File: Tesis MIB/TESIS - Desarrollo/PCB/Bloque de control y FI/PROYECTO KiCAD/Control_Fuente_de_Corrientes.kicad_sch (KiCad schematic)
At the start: 1 part, among them J1 AudioJack2

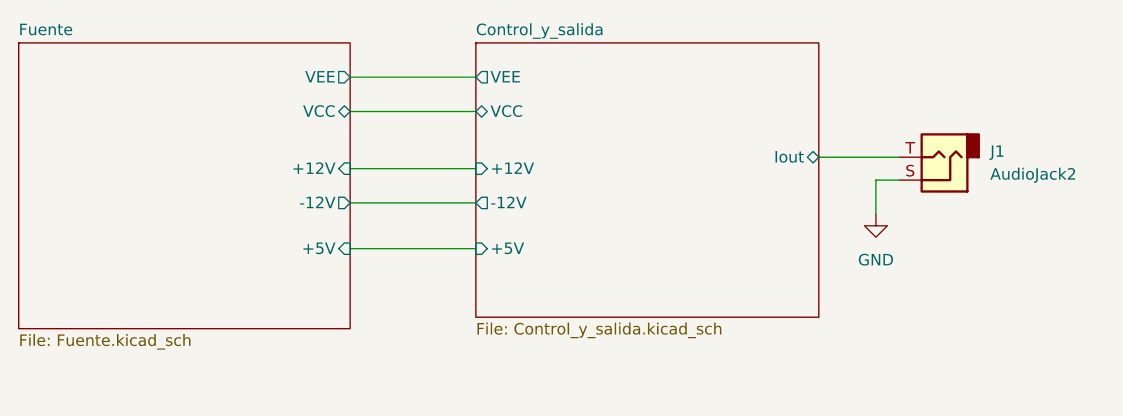
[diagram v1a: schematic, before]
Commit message: Actualiza Pruebas
Agrega planilla, gráficos y capturas del osciloscopio para el CAP3
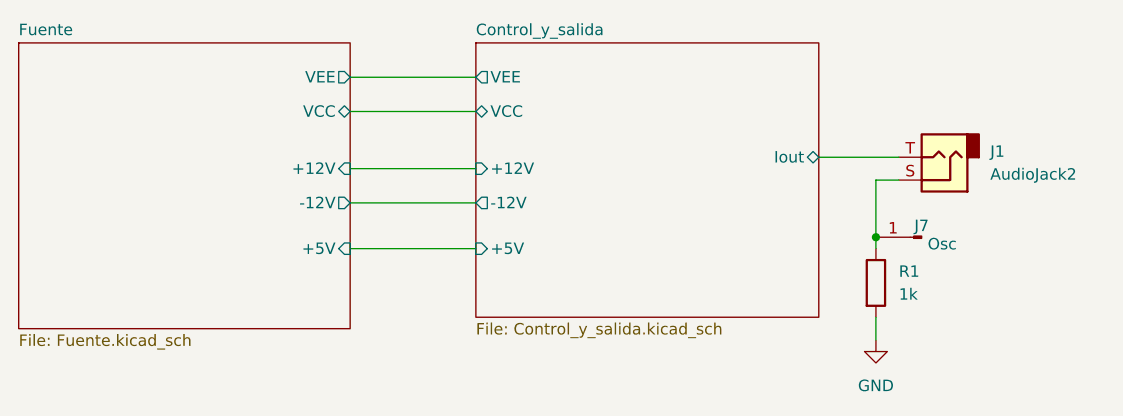
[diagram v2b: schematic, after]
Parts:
- added J7: Osc, Connector_Pin:Pin_D0.9mm_L10.0mm_W2.4mm_FlatFork, symbol Connector:Conn_01x01_Male
- added R1: 1k, Resistor_THT:R_Axial_DIN0207_L6.3mm_D2.5mm_P10.16mm_Horizontal, symbol Device:R
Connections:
- net GND: now also R1.2; no longer J1.S
- new net: J1.S, J7.1 (Pin_1), R1.1
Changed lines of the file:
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@@
 		(comment 2 "Tesis MIB: García Cabrera, Jeremías A.")
 	)
-	(wire
-		(pts
-			(xy 214.63 83.82) (xy 214.63 87.63)
+	(junction
+		(at 214.63 90.17)
+		(diameter 0)
+		(color 0 0 0 0)
+	)
+	(wire
+		(pts
+			(xy 214.63 90.17) (xy 214.63 91.44)
+		)
+		(stroke
+			(width 0)
+			(type default)
+		)
+	)
+	(wire
+		(pts
+			(xy 214.63 99.06) (xy 214.63 101.6)
 		)
 		(stroke
@@
 			(width 0)
 			(type default)
+		)
+	)
+	(wire
+		(pts
+			(xy 214.63 83.82) (xy 214.63 90.17)
+		)
+		(stroke
+			(width 0)
+			(type default)
+		)
+	)
+	(symbol
+		(lib_id "Device:R")
+		(at 214.63 95.25 0)
+		(unit 1)
+		(exclude_from_sim no)
+		(in_bom yes)
+		(on_board yes)
+		(dnp no)
+		(fields_autoplaced yes)
+		(property "Reference" "R1"
+			(at 217.17 93.9799 0)
+			(effects
+				(font
+					(size 1.27 1.27)
+				)
+				(justify left)
+			)
+		)
+		(property "Value" "1k"
+			(at 217.17 96.5199 0)
+			(effects
+				(font
+					(size 1.27 1.27)
+				)
+				(justify left)
+			)
+		)
+		(property "Footprint" "Resistor_THT:R_Axial_DIN0207_L6.3mm_D2.5mm_P10.16mm_Horizontal"
+			(at 212.852 95.25 90)
+			(effects
+				(font
+					(size 1.27 1.27)
+				)
+				(hide yes)
+			)
+		)
+		(property "Datasheet" "~"
+			(at 214.63 95.25 0)
+			(effects
+				(font
+					(size 1.27 1.27)
+				)
+				(hide yes)
+			)
+		)
+		(property "Description" "Shunt"
+			(at 214.63 95.25 0)
+			(effects
+				(font
+					(size 1.27 1.27)
+				)
+				(hide yes)
+			)
+		)
+		(pin "1"
+		)
+		(pin "2"
+		)
+		(instances
+			(project "Control_Fuente_de_Corrientes"
+				(path "/d8b362ed-b66b-443a-9ff8-8e45e9f3933f"
+					(reference "R1")
+					(unit 1)
+				)
+			)
+		)
+	)
+	(symbol
+		(lib_id "Connector:Conn_01x01_Male")
+		(at 219.71 90.17 180)
+		(unit 1)
+		(exclude_from_sim no)
+		(in_bom yes)
+		(on_board yes)
+		(dnp no)
+		(property "Reference" "J7"
+			(at 219.71 88.9 0)
+			(effects
+				(font
+					(size 1.27 1.27)
+				)
+			)
+		)
+		(property "Value" "Osc"
+			(at 221.996 90.932 0)
+			(effects
+				(font
+					(size 1.27 1.27)
+				)
+			)
+		)
+		(property "Footprint" "Connector_Pin:Pin_D0.9mm_L10.0mm_W2.4mm_FlatFork"
+			(at 219.71 90.17 0)
+			(effects
+				(font
+					(size 1.27 1.27)
+				)
+				(hide yes)
+			)
+		)
+		(property "Datasheet" "~"
+			(at 219.71 90.17 0)
+			(effects
+				(font
+					(size 1.27 1.27)
+				)
+				(hide yes)
+			)
+		)
+		(property "Description" "Pin para osciloscopio"
+			(at 219.71 90.17 0)
+			(effects
+				(font
+					(size 1.27 1.27)
+				)
+				(hide yes)
+			)
+		)
+		(pin "1"
+		)
+		(instances
+			(project "Control_Fuente_de_Corrientes"
+				(path "/d8b362ed-b66b-443a-9ff8-8e45e9f3933f"
+					(reference "J7")
+					(unit 1)
+				)
+			)
 		)
 	)
@@
 	(symbol
 		(lib_id "power:GND")
-		(at 214.63 87.63 0)
+		(at 214.63 101.6 0)
 		(unit 1)
 		(exclude_from_sim no)
@@
 		(fields_autoplaced yes)
 		(property "Reference" "#PWR01"
-			(at 214.63 93.98 0)
+			(at 214.63 107.95 0)
 			(effects
 				(font
@@
 		)
 		(property "Value" "GND"
-			(at 214.63 92.71 0)
+			(at 214.63 106.68 0)
 			(effects
 				(font
@@
 		)
 		(property "Footprint" ""
-			(at 214.63 87.63 0)
+			(at 214.63 101.6 0)
 			(effects
 				(font
@@
 		)
 		(property "Datasheet" ""
-			(at 214.63 87.63 0)
+			(at 214.63 101.6 0)
 			(effects
 				(font
@@
 		)
 		(property "Description" ""
-			(at 214.63 87.63 0)
-			(effects
-				(font
+			(at 214.63 101.6 0)
+			(effects
+				(font
